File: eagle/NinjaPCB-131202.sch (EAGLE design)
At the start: 17 parts, among them IC1 MCP3551SN, J2 22--08, Q2 BSS97, Q3 BSS97

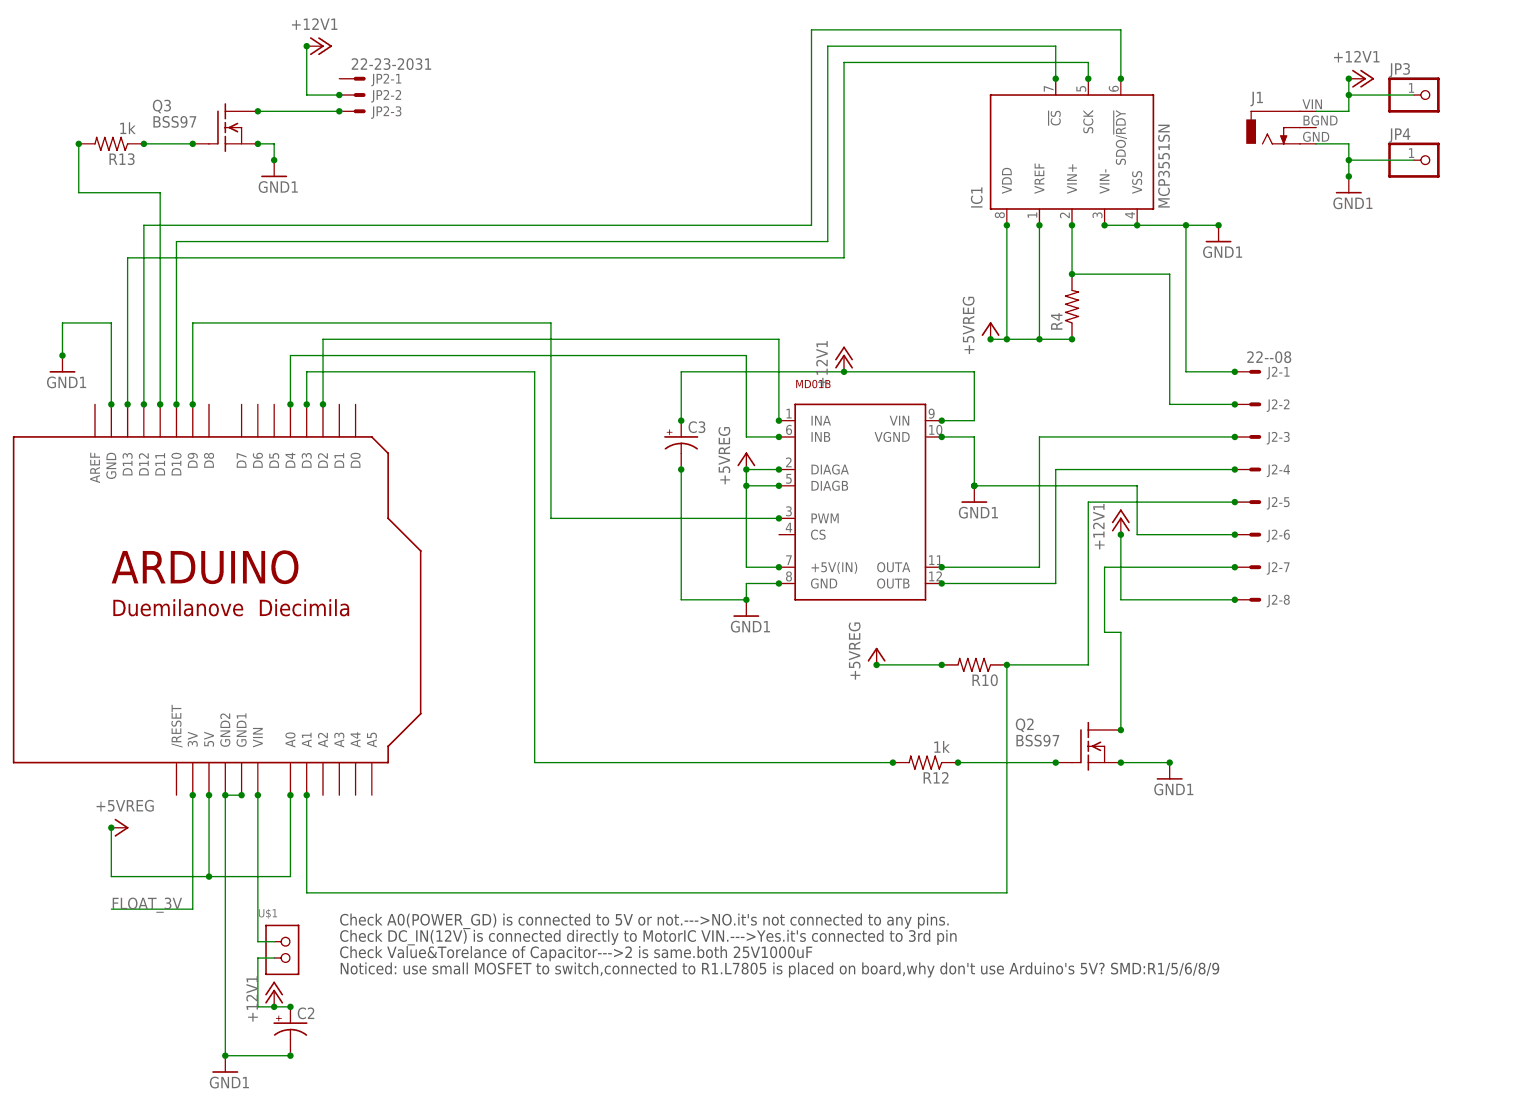
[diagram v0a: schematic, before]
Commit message: add values of reg&cap
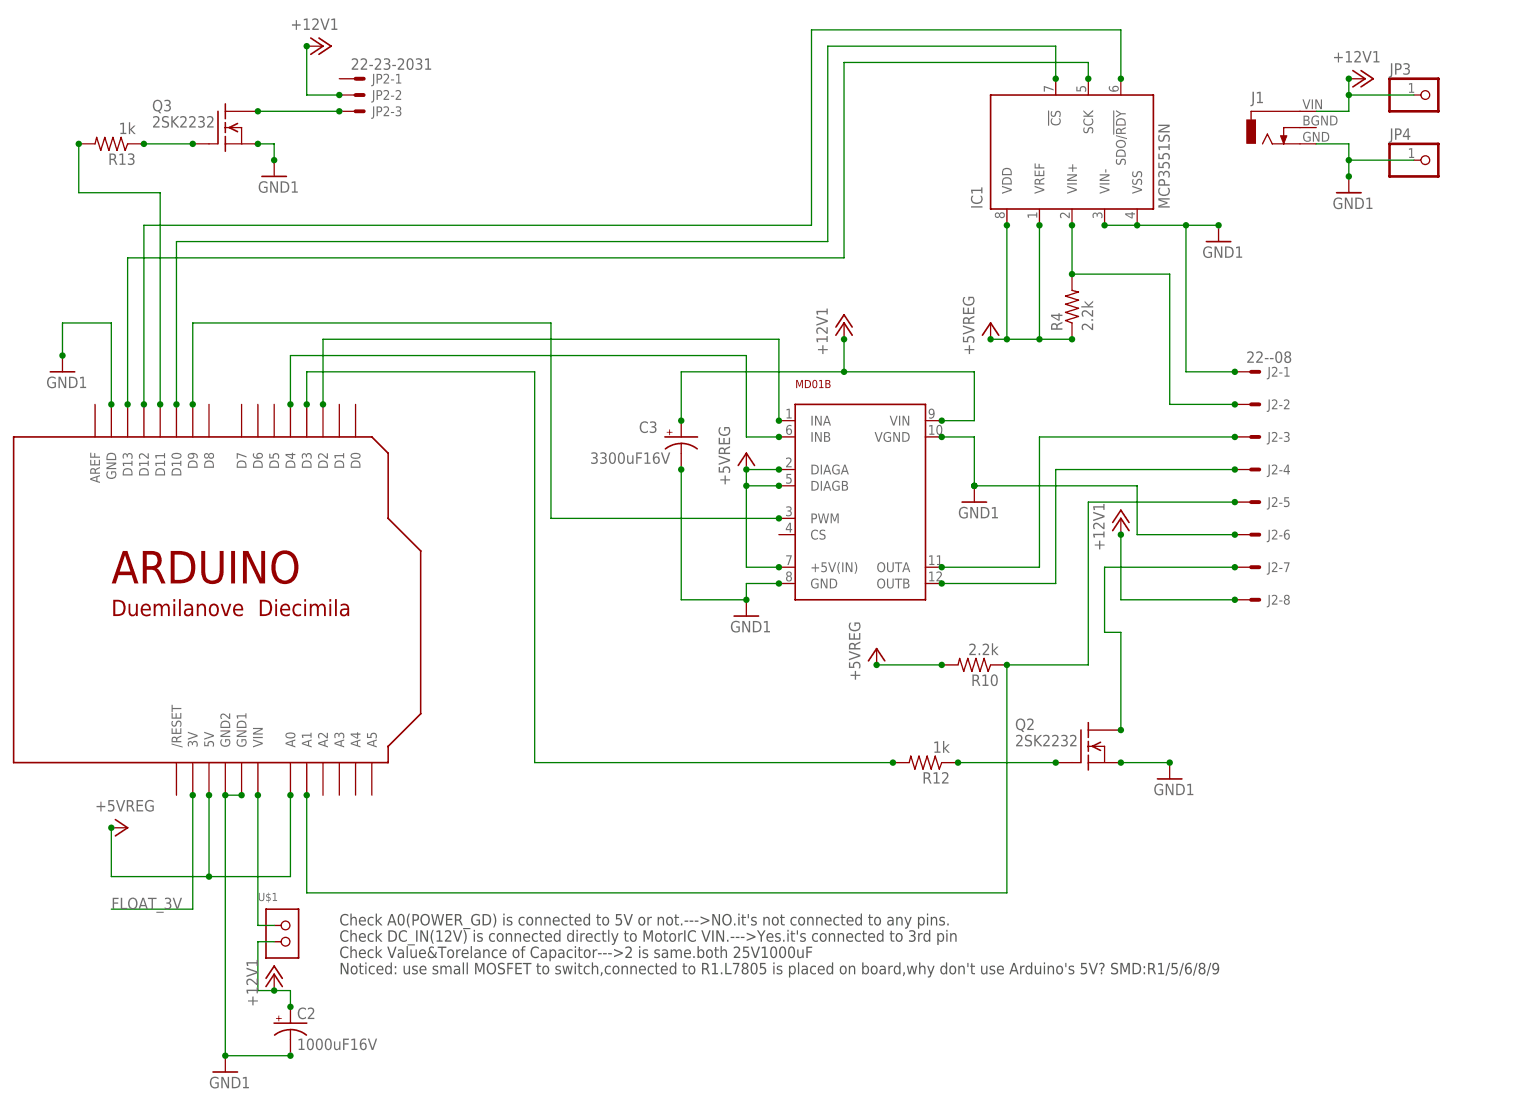
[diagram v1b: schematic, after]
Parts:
- C2: value (none) -> 1000uF16V
- C3: value (none) -> 3300uF16V
- Q2, Q3: value BSS97 -> 2SK2232
- R10, R4: value (none) -> 2.2k
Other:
- moved on the sheet: U$1

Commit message: Use same values in sch and brd
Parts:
- U$3: value ARDUINODUEMILANOVE -> Arduino UNO; device openpcr:ARDUINODUEMILANOVE -> openpcr:ARDUINONS
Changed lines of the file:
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@@
 <part name="GND6" library="openpcr" deviceset="GND1" device=""/>
 <part name="C3" library="rcl" deviceset="CPOL-US" device="E5-13" value="3300uF16V"/>
-<part name="U$3" library="openpcr" deviceset="ARDUINO" device="DUEMILANOVE"/>
+<part name="U$3" library="openpcr" deviceset="ARDUINO" device="NS" value="Arduino UNO"/>
 <part name="IC1" library="microchip" deviceset="MCP355*" device="SN" technology="1"/>
 <part name="P+5" library="openpcr" deviceset="+12V1" device=""/>

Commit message: completed ver2-170831
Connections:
- net N$10 renamed OUTB
- net N$9 renamed OUTA
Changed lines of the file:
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@@
 </segment>
 </net>
-<net name="N$9" class="0">
+<net name="OUTA" class="0">
 <segment>
 <pinref part="MD01B" gate="G$1" pin="OUTA"/>
@@
 </segment>
 </net>
-<net name="N$10" class="0">
+<net name="OUTB" class="0">
 <segment>
 <pinref part="MD01B" gate="G$1" pin="OUTB"/>
